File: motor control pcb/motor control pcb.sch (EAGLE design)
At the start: 81 parts, among them IC1 7805TV, IC2 A3949, IC3 SMS-12, IC4 SN75176ASOIC, IC5 ATMEGA328, IC6 FT232RL, IC7 LM358D, IC8 MAX6675, Q1 PH7030L, Q2 PH7030L, Q3 PH7030L, Q4 16MHZ, T1 BSS84, X1 9090-4V, X5 C-GRID-04-70543, X6 MSTBV10

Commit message: Motor control PCB
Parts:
- removed 12V, 5V, A, B, C, DIR1, RX, TX: (no value), SparkFun:LED0805
- removed C1, C2: 100uF, rcl:CPOL-EUE3.5-8
- removed C10, C11, C16, C17, C18, C19, C3, C4, C5, C6: 100nF, SparkFun:CAP0805
- removed C9: .22uF, SparkFun:CAP0805
- removed IC1: 7805TV, linear:7805TV
- removed IC2: A3949, reprap:A3949
- removed IC3: SMS-12, reprap:TVS-DIODE-ARRAY
- removed IC6: FT232RL, reprap:FT232RL
- removed IC7: LM358D, linear:LM358D
- removed IC8: MAX6675, reprap:MAX6675
- removed JP4: (no value), pinhead:PINHD-1X4
- removed JP6, JP7: (no value), pinhead:PINHD-2X3
- removed L1: 100mA, resistor:L-EUL1812
- removed Q1, Q2, Q3: PH7030L, transistor-power:PH7030L
- removed R10, R20, R21, R5, R6: 4.7K, SparkFun:RESISTOR
- removed R11, R13, R14, R15, R17, R18, R19, R22, R29, R31: 1K, SparkFun:RESISTOR
- removed R12, R4: 10K, SparkFun:RESISTOR
- removed R9: 2.2K, SparkFun:RESISTOR
- removed SPEED1: 1, SparkFun:LED0805
- removed T1: BSS84, zetex:PMOSSOT23
- removed TP3, TP4: PTR1TP09R, testpad:PTR1TP09R
- removed X2: (no value), reprap:USBA
- removed X5: C-GRID-04-70543, reprap:C-GRID-04-70543
- removed X6: MSTBV10, con-phoenix-508:MSTBV10
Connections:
- removed net APWR: A.C, Q3.D, X6-8.1
- removed net BPWR: B.C, Q1.D, X6-6.1
- removed net CPWR: C.C, Q2.D, X6-4.1
- removed net N$1: C5.2, IC8.GND, IC8.T-, X6-9.1
- removed net N$11: C5.1, IC8.T+, X6-10.1
- removed net N$12: IC2.SLEEP, R4.2
- removed net N$18: R11.1, SPEED1.C
- removed net N$2: C.A, R14.1
- removed net N$23: DIR1.C, R13.2
- removed net N$25: 5V.A, R15.1
- removed net N$26: 12V.A, R9.1
- removed net N$29: IC6.USBDP, X2.3
- removed net N$3: C9.2, IC2.VREG
- removed net N$30: IC6.USBDM, X2.2
- removed net N$36: C18.1, IC6.RESET#
- removed net N$37: L1.2, X2.1
- removed net N$38: C16.2, IC6.VCC30
- removed net N$39: R19.2, RX.A
- removed net N$4: IC2.OUTA, IC3.D4, X6-1.1
- removed net N$40: R22.2, TX.A
- removed net N$41: A.A, R31.1
- removed net N$42: B.A, R29.1
- removed net N$44: IC6.GPIO1, RX.C
- removed net N$45: IC6.GPIO0, TX.C
- removed net N$46: C19.1, IC6.DTR#
- removed net N$47: IC6.TXD, R17.2
- removed net N$48: IC6.RXD, R18.2
- removed net N$5: IC2.OUTB, IC3.D3, X6-2.1
- removed net N$50: IC7A.OUT, IC7B.+IN
- removed net N$51: IC7B.-IN, IC7B.OUT, T1.G
- removed net N$6: C10.2, IC2.CP2
- removed net N$7: C10.1, IC2.CP1
- removed net N$9: C11.1, IC2.VCP
- removed net USBVCC: C17.2, IC6.VCC5I, IC6.VCCIO, IC7A.-IN, L1.1, R19.1, R22.1, T1.D, TP3.TP
- net +12V: no longer C1.+, C11.2, C3.1, IC1.VI, IC2.VBB, IC7A.+IN, R14.2, R29.2, R31.2, R9.2, X6-3.1, X6-5.1, X6-7.1
- net A2: no longer JP6.6
- net A3: no longer JP6.5
- net A6: no longer JP7.6
- net A7: no longer JP7.5
- net D10: no longer Q3.G, R5.2
- net D12: no longer IC8.SO
- net D13: no longer IC8.SCK
- net D2: no longer X5-3.S
- net D3: no longer X5-4.S
- net D4: no longer IC8.CS, R12.1
- net D5: no longer IC2.ENABLE, SPEED1.A
- net D6: no longer Q2.G, R10.2
- net D8: no longer DIR1.A, IC2.PHASE/DIR
- net D9: no longer Q1.G, R6.2
- net GND: no longer 12V.C, 5V.C, C1.-, C16.1, C17.1, C18.2, C2.-, C3.2, C4.2, C6.1, C9.1, IC1.GND, IC2.GND, IC2.GND1, IC2.MODE, IC2.SENSE, IC3.GND1, IC3.GND2, IC6.AGND, IC6.GND1, IC6.GND2, IC6.GND3, IC6.TEST, JP4.2, JP6.1, JP6.2, JP7.1, JP7.2, Q1.S, Q1.S@1, Q1.S@2, Q2.S, Q2.S@1, Q2.S@2, Q3.S, Q3.S@1, Q3.S@2, R10.1, R11.2, R13.1, R5.1, R6.1, X2.4, X2.P$1, X2.P$2, X5-2.S
- net RESET: no longer C19.2
- net RX: no longer R17.1
- net SCL: no longer JP4.4, R21.1
- net SDA: no longer JP4.3, R20.1
- net TX: no longer R18.1
- net VCC: no longer C2.+, C4.1, C6.2, IC1.VO, IC8.VCC, JP4.1, JP6.3, JP6.4, JP7.3, JP7.4, R12.2, R15.2, R20.2, R21.2, R4.1, T1.S, TP4.TP, X5-1.S
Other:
- note removed: "......."
- note removed: "A"
- note removed: "B"
- note removed: "C"
- note removed: "DC MOTOR DRIVER"
- note removed: "EXTRA ANALOG"
- note removed: "Extruder Controller v3.5"
- note removed: "I2C"
- note removed: "MOSFETS"
- note removed: "Note: Do not use poly to gnd pins 1 and 2"
- note removed: "POWER SUPPLY"
- note removed: "QUADRATURE"
- note removed: "THERMOCOUPLE"
- note removed: "USB to SERIAL"
- note removed: "wiki.makerbot.com/ec3"

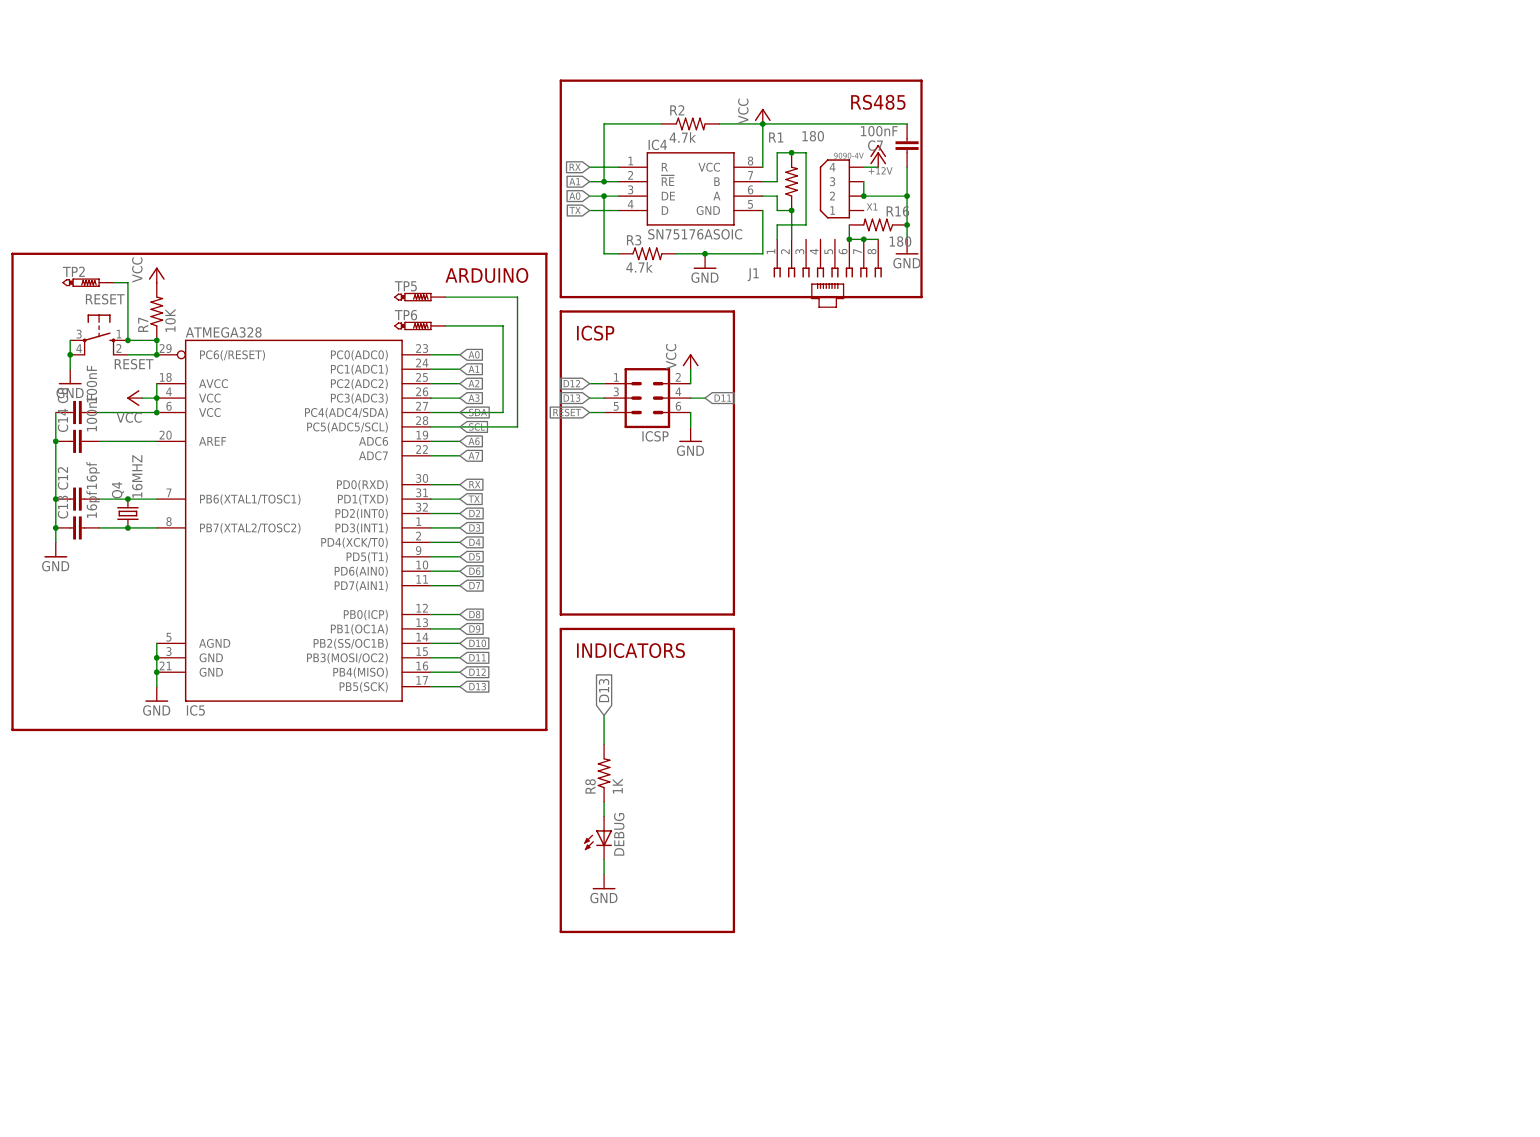
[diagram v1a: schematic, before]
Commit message: Rev 0 of the motor control pcb; update for smaller traces.
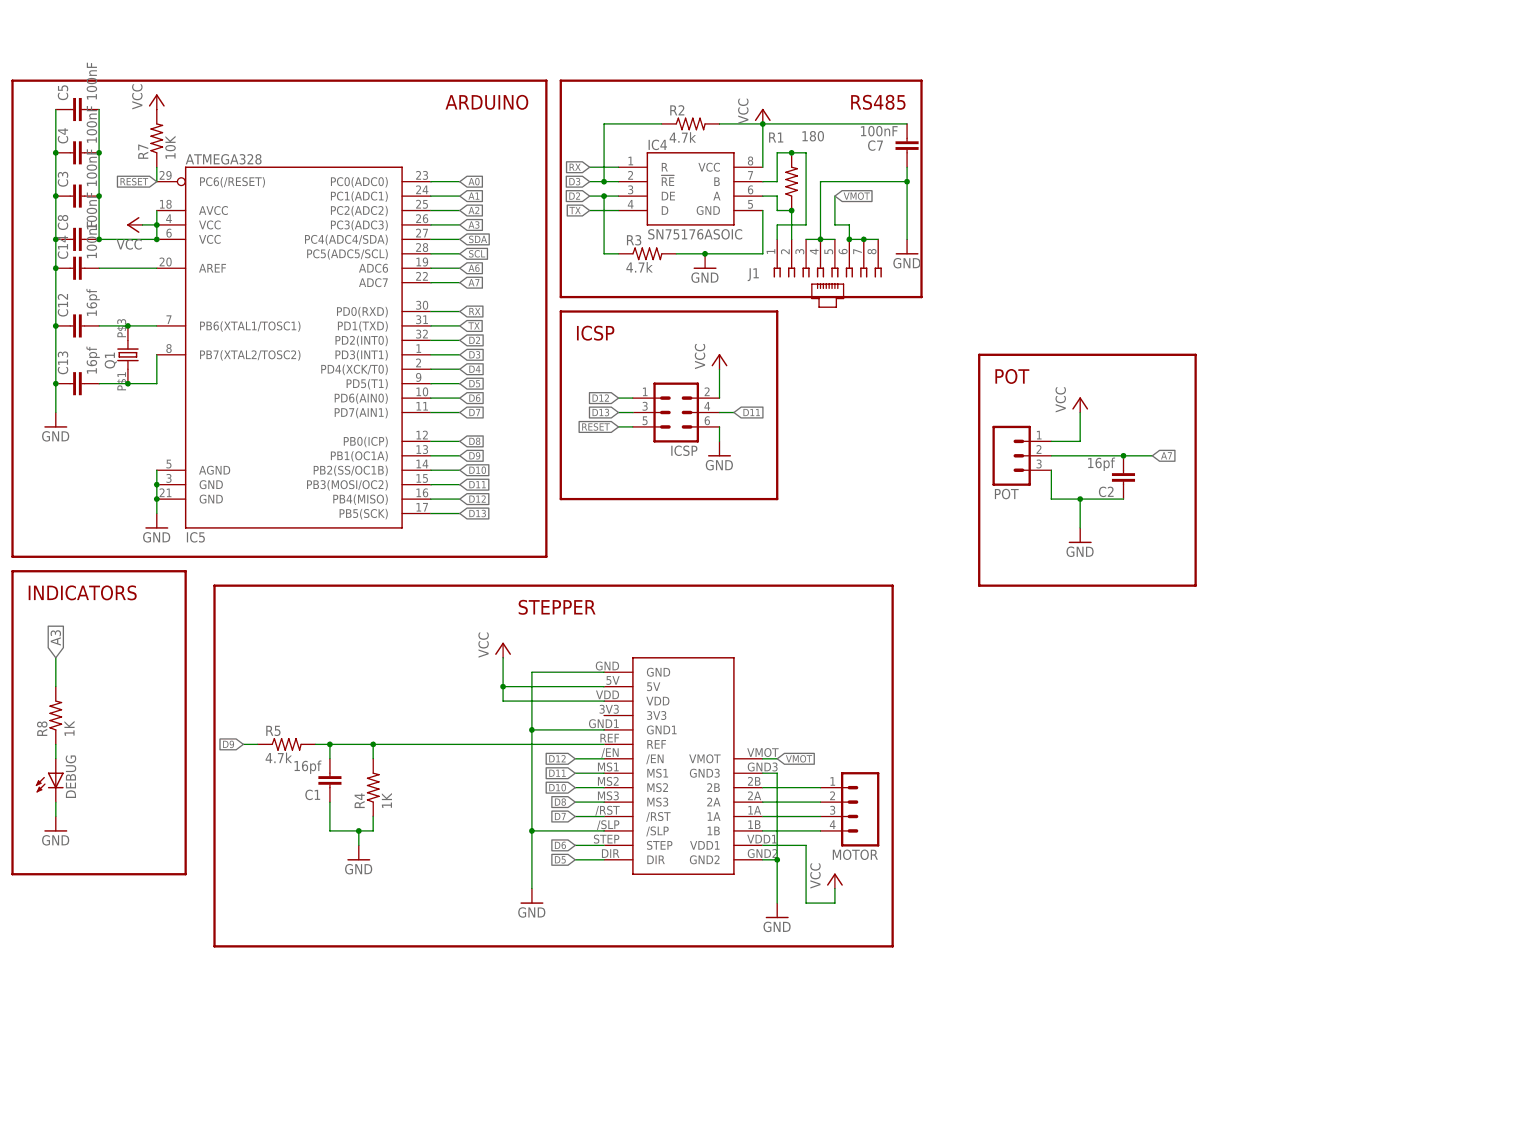
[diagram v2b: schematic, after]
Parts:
- removed Q4: 16MHZ, crystal:CRYSTALHC49S
- removed R16: 180, SparkFun:RESISTOR
- removed RESET: (no value), switch-omron:10-XX
- removed TP2, TP5, TP6: PTR1TP09R, testpad:PTR1TP09R
- removed X1: 9090-4V, con-thomas-betts:9090-4V
- added C1, C2: 16pf, SparkFun:CAP0805
- added C3, C4, C5: 100nF, SparkFun:CAP0805
- added MOTOR: (no value), SparkFun:M04PTH
- added POT: (no value), SparkFun:M03PTH
- added Q1: (no value), blinkyboard:GLOWBOARD_ABMM2
- added R4: 1K, SparkFun:RESISTOR
- added R5: 4.7k, SparkFun:RESISTOR
- added U$1: POLOLU_DRIVER, sonos_library:POLOLU_DRIVER
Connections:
- removed net +12V: X1.4
- removed net N$32: C13.2, IC5.PB7(XTAL2/TOSC2), Q4.1
- removed net N$83: J1.6, J1.7, J1.8, R16.2
- new net N$11: C1.2, R4.2, R5.2, U$1.REF
- new net N$2: MOTOR.1, U$1.2B
- new net N$3: MOTOR.2, U$1.2A
- new net N$4: MOTOR.3, U$1.1A
- new net N$5: MOTOR.4, U$1.1B
- new net N$6: C13.2, IC5.PB7(XTAL2/TOSC2), Q1.1
- new net VMOT: J1.6, J1.7, J1.8, U$1.VMOT
- net A0: no longer IC4.DE, R3.1
- net A1: no longer IC4.!RE, R2.1
- net A3: now also R8.2
- net A7: now also C2.2, POT.2
- net D10: now also U$1.MS2
- net D11: now also U$1.MS1
- net D12: now also U$1./EN
- net D13: no longer R8.2
- net D2: now also IC4.DE, R3.1
- net D3: now also IC4.!RE, R2.1
- net D5: now also U$1.DIR
- net D6: now also U$1.STEP
- net D7: now also U$1./RST
- net D8: now also U$1.MS3
- net D9: now also R5.1
- net GND: now also C1.1, C2.1, C3.1, C4.1, C5.1, J1.3, J1.4, J1.5, POT.3, R4.1, U$1./SLP, U$1.GND, U$1.GND1, U$1.GND2, U$1.GND3; no longer R16.1, RESET.P, RESET.P1, X1.2, X1.3
- net N$31: now also Q1.2; no longer Q4.2
- net RESET: no longer RESET.S, RESET.S1, TP2.TP
- net SCL: no longer TP5.TP
- net SDA: no longer TP6.TP
- net VCC: now also C3.2, C4.2, C5.2, POT.1, U$1.5V, U$1.VDD, U$1.VDD1
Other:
- note added: "POT"
- note added: "STEPPER"
- moved on the sheet: C12, C13, C14, C8, DEBUG, IC5, ICSP, R7, R8

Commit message: Board layout finished, need verification
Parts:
- added C6: ?pf, SparkFun:CAP0805
- C1, C2: value 16pf -> ?pf
- C8: value 100nF -> ?pf; device SparkFun:CAP0805 -> SparkFun:CAP1210
- R2, R3: value 4.7k -> 10k
- R4: value 1K -> ?k
- R5: value 4.7k -> ?k
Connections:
- net GND: now also C6.1
- net VCC: no longer C8.2
- net VMOT: now also C6.2, C8.2
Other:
- note added: "INDICATOR"
- note removed: "INDICATORS"
- moved on the sheet: C8
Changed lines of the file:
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@@
 <part name="GND2" library="SparkFun" deviceset="GND" device=""/>
 <part name="R1" library="SparkFun" deviceset="RESISTOR" device="" value="180"/>
-<part name="R2" library="SparkFun" deviceset="RESISTOR" device="" value="4.7k"/>
-<part name="R3" library="SparkFun" deviceset="RESISTOR" device="" value="4.7k"/>
+<part name="R2" library="SparkFun" deviceset="RESISTOR" device="" value="10k"/>
+<part name="R3" library="SparkFun" deviceset="RESISTOR" device="" value="10k"/>
 <part name="IC5" library="SparkFun" deviceset="ATMEGA168" device="" value="ATMEGA328"/>
 <part name="P+2" library="supply1" deviceset="VCC" device=""/>
@@
 <part name="P+18" library="supply1" deviceset="VCC" device=""/>
 <part name="C7" library="SparkFun" deviceset="CAP" device="0805" value="100nF"/>
-<part name="C8" library="SparkFun" deviceset="CAP" device="0805" value="100nF"/>
 <part name="GND4" library="SparkFun" deviceset="GND" device=""/>
 <part name="GND8" library="SparkFun" deviceset="GND" device=""/>
@@
 <part name="P+3" library="supply1" deviceset="VCC" device=""/>
 <part name="GND5" library="supply1" deviceset="GND" device=""/>
-<part name="R4" library="SparkFun" deviceset="RESISTOR" device="" value="1K"/>
-<part name="C1" library="SparkFun" deviceset="CAP" device="0805" value="16pf"/>
-<part name="R5" library="SparkFun" deviceset="RESISTOR" device="" value="4.7k"/>
+<part name="R4" library="SparkFun" deviceset="RESISTOR" device="" value="?k"/>
+<part name="C1" library="SparkFun" deviceset="CAP" device="0805" value="?pf"/>
+<part name="R5" library="SparkFun" deviceset="RESISTOR" device="" value="?k"/>
 <part name="GND6" library="supply1" deviceset="GND" device=""/>
 <part name="POT" library="SparkFun" deviceset="M03" device="PTH"/>
@@
 <part name="P+4" library="supply1" deviceset="VCC" device=""/>
 <part name="GND7" library="SparkFun" deviceset="GND" device=""/>
-<part name="C2" library="SparkFun" deviceset="CAP" device="0805" value="16pf"/>
+<part name="C2" library="SparkFun" deviceset="CAP" device="0805" value="?pf"/>
 <part name="Q1" library="blinkyboard" deviceset="GLOWBOARD_ABMM2" device=""/>
 <part name="C3" library="SparkFun" deviceset="CAP" device="0805" value="100nF"/>
 <part name="C4" library="SparkFun" deviceset="CAP" device="0805" value="100nF"/>
 <part name="C5" library="SparkFun" deviceset="CAP" device="0805" value="100nF"/>
+<part name="C6" library="SparkFun" deviceset="CAP" device="0805" value="?pf"/>
+<part name="C8" library="SparkFun" deviceset="CAP" device="1210" value="?pf"/>
 </parts>
 <sheets>
@@
 <text x="104.14" y="33.02" size="2.54" layer="94">ICSP</text>
 <text x="81.28" y="73.66" size="2.54" layer="94">ARDUINO</text>
-<text x="7.62" y="-12.7" size="2.54" layer="94">INDICATORS</text>
+<text x="7.62" y="-12.7" size="2.54" layer="94">INDICATOR</text>
 <text x="93.98" y="-15.24" size="2.54" layer="94">STEPPER</text>
 <wire x1="5.08" y1="78.74" x2="5.08" y2="-5.08" width="0.4064" layer="94"/>
@@
 <attribute name="VALUE" x="161.036" y="70.739" size="1.778" layer="96" rot="R180"/>
 </instance>
-<instance part="C8" gate="G$1" x="17.78" y="50.8" rot="R90"/>
 <instance part="GND4" gate="1" x="30.48" y="0"/>
 <instance part="GND8" gate="1" x="162.56" y="48.26"/>
@@
 <instance part="C4" gate="G$1" x="17.78" y="66.04" rot="R90"/>
 <instance part="C5" gate="G$1" x="17.78" y="73.66" rot="R90"/>
+<instance part="C6" gate="G$1" x="142.24" y="-33.02" rot="R180"/>
+<instance part="C8" gate="G$1" x="149.86" y="-33.02" rot="R180"/>
 </instances>
 <busses>
@@
 <wire x1="12.7" y1="25.4" x2="12.7" y2="20.32" width="0.1524" layer="91"/>
 <wire x1="12.7" y1="45.72" x2="12.7" y2="35.56" width="0.1524" layer="91"/>
-<wire x1="12.7" y1="50.8" x2="12.7" y2="45.72" width="0.1524" layer="91"/>
 <junction x="12.7" y="25.4"/>
 <junction x="12.7" y="35.56"/>
-<junction x="12.7" y="45.72"/>
 <pinref part="C12" gate="G$1" pin="1"/>
 <pinref part="C13" gate="G$1" pin="1"/>
 <pinref part="GND3" gate="1" pin="GND"/>
 <pinref part="C14" gate="G$1" pin="1"/>
-<pinref part="C8" gate="G$1" pin="1"/>
+<pinref part="C3" gate="G$1" pin="1"/>
 <pinref part="C4" gate="G$1" pin="1"/>
-<pinref part="C3" gate="G$1" pin="1"/>
-<wire x1="12.7" y1="66.04" x2="12.7" y2="58.42" width="0.1524" layer="91"/>
-<wire x1="12.7" y1="58.42" x2="12.7" y2="50.8" width="0.1524" layer="91"/>
-<junction x="12.7" y="58.42"/>
-<junction x="12.7" y="50.8"/>
 <pinref part="C5" gate="G$1" pin="1"/>
 <wire x1="12.7" y1="73.66" x2="12.7" y2="66.04" width="0.1524" layer="91"/>
 <junction x="12.7" y="66.04"/>
+<wire x1="12.7" y1="66.04" x2="12.7" y2="58.42" width="0.1524" layer="91"/>
+<wire x1="12.7" y1="58.42" x2="12.7" y2="45.72" width="0.1524" layer="91"/>
+<junction x="12.7" y="58.42"/>
+<junction x="12.7" y="45.72"/>
 </segment>
 <segment>
@@
 <wire x1="139.7" y1="-43.18" x2="139.7" y2="-58.42" width="0.1524" layer="91"/>
 <junction x="139.7" y="-58.42"/>
+<pinref part="C8" gate="G$1" pin="1"/>
+<wire x1="149.86" y1="-40.64" x2="149.86" y2="-38.1" width="0.1524" layer="91"/>
+<pinref part="C6" gate="G$1" pin="1"/>
+<wire x1="142.24" y1="-40.64" x2="142.24" y2="-38.1" width="0.1524" layer="91"/>
+<wire x1="142.24" y1="-40.64" x2="149.86" y2="-40.64" width="0.1524" layer="91"/>
+<wire x1="139.7" y1="-43.18" x2="142.24" y2="-43.18" width="0.1524" layer="91"/>
+<wire x1="142.24" y1="-43.18" x2="142.24" y2="-40.64" width="0.1524" layer="91"/>
+<junction x="142.24" y="-40.64"/>
+<junction x="139.7" y="-43.18"/>
 </segment>
 <segment>
@@
 <pinref part="IC5" gate="G$1" pin="AVCC"/>
 <pinref part="P+18" gate="VCC" pin="VCC"/>
-<pinref part="C8" gate="G$1" pin="2"/>
 <pinref part="C4" gate="G$1" pin="2"/>
 <pinref part="C3" gate="G$1" pin="2"/>
 <wire x1="20.32" y1="66.04" x2="20.32" y2="58.42" width="0.1524" layer="91"/>
 <wire x1="20.32" y1="58.42" x2="20.32" y2="50.8" width="0.1524" layer="91"/>
-<junction x="20.32" y="50.8"/>
 <junction x="20.32" y="58.42"/>
 <pinref part="C5" gate="G$1" pin="2"/>
@@
 <net name="VMOT" class="0">
 <segment>
+<label x="137.16" y="-22.86" size="1.27" layer="95" xref="yes"/>
+<wire x1="137.16" y1="-27.94" x2="137.16" y2="-22.86" width="0.1524" layer="91"/>
+<pinref part="C6" gate="G$1" pin="2"/>
+<wire x1="137.16" y1="-27.94" x2="142.24" y2="-27.94" width="0.1524" layer="91"/>
+<wire x1="142.24" y1="-27.94" x2="142.24" y2="-30.48" width="0.1524" layer="91"/>
+<pinref part="C8" gate="G$1" pin="2"/>
+<wire x1="142.24" y1="-27.94" x2="149.86" y2="-27.94" width="0.1524" layer="91"/>
+<wire x1="149.86" y1="-27.94" x2="149.86" y2="-30.48" width="0.1524" layer="91"/>
 <pinref part="U$1" gate="G$1" pin="VMOT"/>
-<wire x1="137.16" y1="-40.64" x2="139.7" y2="-40.64" width="0.1524" layer="91"/>
-<label x="139.7" y="-40.64" size="1.27" layer="95" xref="yes"/>
-</segment>
-<segment>
+<wire x1="137.16" y1="-27.94" x2="137.16" y2="-40.64" width="0.1524" layer="91"/>
+<junction x="142.24" y="-27.94"/>
+<junction x="137.16" y="-27.94"/>
+</segment>
+<segment>

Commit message: Finish laying out and verifying board. Bugfix: don't pull /sleep low.
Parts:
- removed ICSP: (no value), con-harting-ml:ML6
- added U$2: 2X3HEADER, sonos_library:2X3HEADER
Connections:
- net A3: no longer R8.2
- net D11: now also U$2.4; no longer ICSP.4
- net D12: now also U$2.1; no longer ICSP.1
- net D13: now also U$2.3; no longer ICSP.3
- net D4: now also R8.2
- net GND: now also U$2.6; no longer ICSP.6, U$1./SLP
- net RESET: now also U$2.5; no longer ICSP.5
- net VCC: now also U$1./SLP, U$2.2; no longer ICSP.2
